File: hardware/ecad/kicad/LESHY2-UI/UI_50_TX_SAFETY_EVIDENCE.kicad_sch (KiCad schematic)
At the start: 0 parts

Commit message: complete exact H2.2.9 UI TX safety schematic
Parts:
- added C1: TDK C1005X7R1H104K050BB, Capacitor_SMD:C_0402_1005Metric, symbol Leshy2:UI50_IR_EVIDENCE_AMP_BYPASS
- added C2: TDK C1005X7R1H104K050BB, Capacitor_SMD:C_0402_1005Metric, symbol Leshy2:UI50_IR_EVIDENCE_VREF_CAP
- added C3: KEMET C0402C102K5RACTU, Capacitor_SMD:C_0402_1005Metric, symbol Leshy2:UI50_IR_EVIDENCE_FEEDBACK_CAP
- added C4: TDK C1005X7R1H104K050BB, Capacitor_SMD:C_0402_1005Metric, symbol Leshy2:UI50_EVIDENCE_CMP_A_BYPASS
- added D1: VEMD1060X01, Leshy2:VEMD1060X01, symbol Leshy2:UI50_DET_IR
- added Q1: Diodes Incorporated 2N7002DW-7-F, Package_TO_SOT_SMD:SOT-363_SC-70-6, symbol Leshy2:UI50_SAFE_RESET_SINK_A
- added R1: Yageo RC0402FR-07100KL, Resistor_SMD:R_0402_1005Metric, symbol Leshy2:UI50_IR_EVIDENCE_VREF_TOP
- added R10: Yageo RC0402FR-0710KL, Resistor_SMD:R_0402_1005Metric, symbol Leshy2:UI50_C5_EVIDENCE_THRESHOLD_BOTTOM
- added R11: Yageo RC0402FR-071ML, Resistor_SMD:R_0402_1005Metric, symbol Leshy2:UI50_C5_EVIDENCE_HYSTERESIS
- added R12: Yageo RC0402FR-0710KL, Resistor_SMD:R_0402_1005Metric, symbol Leshy2:UI50_C5_EVIDENCE_OUTPUT_PULLUP
- added R13: Yageo RC0402FR-07100KL, Resistor_SMD:R_0402_1005Metric, symbol Leshy2:UI50_IR_EVIDENCE_THRESHOLD_TOP
- added R14: Yageo RC0402FR-0712KL, Resistor_SMD:R_0402_1005Metric, symbol Leshy2:UI50_IR_EVIDENCE_THRESHOLD_BOTTOM
- added R15: Yageo RC0402FR-071ML, Resistor_SMD:R_0402_1005Metric, symbol Leshy2:UI50_IR_EVIDENCE_HYSTERESIS
- added R16: Yageo RC0402FR-0710KL, Resistor_SMD:R_0402_1005Metric, symbol Leshy2:UI50_IR_EVIDENCE_OUTPUT_PULLUP
- added R17: Yageo RC0402FR-0710KL, Resistor_SMD:R_0402_1005Metric, symbol Leshy2:UI50_C5_EVIDENCE_MAIN_PULLUP
- added R18: Yageo RC0402FR-0710KL, Resistor_SMD:R_0402_1005Metric, symbol Leshy2:UI50_IR_EVIDENCE_MAIN_PULLUP
- added R2: Yageo RC0402FR-0710KL, Resistor_SMD:R_0402_1005Metric, symbol Leshy2:UI50_IR_EVIDENCE_VREF_BOTTOM
- added R3: Yageo RC0402FR-0747KL, Resistor_SMD:R_0402_1005Metric, symbol Leshy2:UI50_IR_EVIDENCE_FEEDBACK
- added R4: Yageo RC0402FR-0710KL, Resistor_SMD:R_0402_1005Metric, symbol Leshy2:UI50_S3_RESET_GATE_PULLUP
- added R5: Yageo RC0402FR-07100KL, Resistor_SMD:R_0402_1005Metric, symbol Leshy2:UI50_S3_EVIDENCE_THRESHOLD_TOP
- added R6: Yageo RC0402FR-0710KL, Resistor_SMD:R_0402_1005Metric, symbol Leshy2:UI50_S3_EVIDENCE_THRESHOLD_BOTTOM
- added R7: Yageo RC0402FR-071ML, Resistor_SMD:R_0402_1005Metric, symbol Leshy2:UI50_S3_EVIDENCE_HYSTERESIS
- added R8: Yageo RC0402FR-0710KL, Resistor_SMD:R_0402_1005Metric, symbol Leshy2:UI50_S3_EVIDENCE_OUTPUT_PULLUP
- added R9: Yageo RC0402FR-07100KL, Resistor_SMD:R_0402_1005Metric, symbol Leshy2:UI50_C5_EVIDENCE_THRESHOLD_TOP
- added U1: TLV9061IDBVR, Package_TO_SOT_SMD:SOT-23-5, symbol Leshy2:UI50_IR_EVIDENCE_AMP
- added U2: LTC5532ES6#TRMPBF, Package_TO_SOT_SMD:TSOT-23-6, symbol Leshy2:UI50_DET_S3
- added U3: LTC5532ES6#TRMPBF, Package_TO_SOT_SMD:TSOT-23-6, symbol Leshy2:UI50_DET_C5
- added U4: TLV1824PWR, Package_SO:TSSOP-14_4.4x5mm_P0.65mm, symbol Leshy2:UI50_EVIDENCE_CMP_A
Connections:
- net 3V3_MAIN: now also R17.1 (END_1), R18.1 (END_1), R4.1 (END_1)
- net AON_SAFE_3V3: now also C1.1 (END_1), C4.1 (END_1), R1.1 (END_1), R12.1 (END_1), R13.1 (END_1), R16.1 (END_1), R5.1 (END_1), R8.1 (END_1), R9.1 (END_1), U1.5 (V_PLUS), U2.6 (VCC), U3.6 (VCC), U4.3 (VPLUS)
- net C5_DETECT_V: now also U3.5 (VOUT), U4.6 (IN2_N)
- net C5_DETECT_VM: now also U3.4 (VM)
- net C5_FORWARD_RF_SAMPLE: now also U3.1 (RFIN)
- net C5_RESET_N: now also Q1.1 (D2)
- net C5_RF_TX_EVIDENCE_N: now also R17.2 (END_2)
- net EV_N0_S3: now also R7.1 (END_1), R8.2 (END_2), U4.2 (OUT1)
- net EV_N1_C5: now also R11.1 (END_1), R12.2 (END_2), U4.1 (OUT2)
- net EV_N7_IR: now also R15.1 (END_1), R16.2 (END_2), U4.14 (OUT3)
- net IR_TX_EVIDENCE_N: now also R18.2 (END_2)
- net RF_RESET_KILL_GATE: now also Q1.5 (G2)
- net S3_DETECT_V: now also U2.5 (VOUT), U4.4 (IN1_N)
- net S3_DETECT_VM: now also U2.4 (VM)
- net S3_FORWARD_RF_SAMPLE: now also U2.1 (RFIN)
- net S3_RESET_KILL_GATE: now also Q1.2 (G1), R4.2 (END_2)
- net S3_RESET_N: now also Q1.4 (D1)
- net SAFETY_GROUND: now also C1.2 (END_2), C2.2 (END_2), C4.2 (END_2), D1.1 (ANODE), Q1.3 (S1), Q1.6 (S2), R10.2 (END_2), R14.2 (END_2), R2.2 (END_2), R6.2 (END_2), U1.2 (V_MINUS), U2.2 (GND), U2.3 (VOS), U3.2 (GND), U3.3 (VOS), U4.10 (IN4_N), U4.11 (IN4_P), U4.12 (VMINUS)
- new net EV_THRESH_0_S3: R5.2 (END_2), R6.1 (END_1), R7.2 (END_2), U4.5 (IN1_P)
- new net EV_THRESH_1_C5: R10.1 (END_1), R11.2 (END_2), R9.2 (END_2), U4.7 (IN2_P)
- new net EV_THRESH_7_IR: R13.2 (END_2), R14.1 (END_1), R15.2 (END_2), U4.9 (IN3_P)
- new net IR_DETECT_V: C3.1 (END_1), R3.1 (END_1), U1.1 (OUT), U4.8 (IN3_N)
- new net IR_EVIDENCE_VREF: C2.1 (END_1), R1.2 (END_2), R2.1 (END_1), U1.3 (IN_PLUS)
- new net IR_OPTICAL_SUM: C3.2 (END_2), D1.2 (CATHODE), R3.2 (END_2), U1.4 (IN_MINUS)
- no-connect marks 19 -> 1
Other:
- title: (none) -> Leshy2 — exact UI-side actual-TX evidence and reset safety

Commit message: complete H2 schematic review package
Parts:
- renumbered C1 to C50001, C2 to C50002, C3 to C50003, C4 to C50004, D1 to D50001, Q1 to Q50001, R1 to R50001, R2 to R50002, R3 to R50003, R4 to R50004, R5 to R50005, R6 to R50006, R7 to R50007, R8 to R50008, R9 to R50009, R10 to R50010, R11 to R50011, R12 to R50012, R13 to R50013, R14 to R50014, R15 to R50015, R16 to R50016, R17 to R50017, R18 to R50018, U1 to U50001, U2 to U50002, U3 to U50003, U4 to U50004
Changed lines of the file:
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@@
 		(on_board yes)
 		(dnp no)
-		(property "Reference" "U1"
+		(property "Reference" "U50001"
 			(at 50.80 40.64 0)
 			(show_name no)
@@
 			(project "LESHY2-UI"
 				(path "/25ddd286-5916-5146-b4db-5f80ff4b0f07"
-					(reference "U1")
+					(reference "U50001")
 					(unit 1)
 				)
@@
 		(on_board yes)
 		(dnp no)
-		(property "Reference" "C1"
+		(property "Reference" "C50001"
 			(at 132.08 39.37 0)
 			(show_name no)
@@
 			(project "LESHY2-UI"
 				(path "/25ddd286-5916-5146-b4db-5f80ff4b0f07"
-					(reference "C1")
+					(reference "C50001")
 					(unit 1)
 				)
@@
 		(on_board yes)
 		(dnp no)
-		(property "Reference" "R1"
+		(property "Reference" "R50001"
 			(at 213.36 39.37 0)
 			(show_name no)
@@
 			(project "LESHY2-UI"
 				(path "/25ddd286-5916-5146-b4db-5f80ff4b0f07"
-					(reference "R1")
+					(reference "R50001")
 					(unit 1)
 				)
@@
 		(on_board yes)
 		(dnp no)
-		(property "Reference" "R2"
+		(property "Reference" "R50002"
 			(at 294.64 39.37 0)
 			(show_name no)
@@
 			(project "LESHY2-UI"
 				(path "/25ddd286-5916-5146-b4db-5f80ff4b0f07"
-					(reference "R2")
+					(reference "R50002")
 					(unit 1)
 				)
@@
 		(on_board yes)
 		(dnp no)
-		(property "Reference" "C2"
+		(property "Reference" "C50002"
 			(at 375.92 39.37 0)
 			(show_name no)
@@
 			(project "LESHY2-UI"
 				(path "/25ddd286-5916-5146-b4db-5f80ff4b0f07"
-					(reference "C2")
+					(reference "C50002")
 					(unit 1)
 				)
@@
 		(on_board yes)
 		(dnp no)
-		(property "Reference" "R3"
+		(property "Reference" "R50003"
 			(at 457.20 39.37 0)
 			(show_name no)
@@
 			(project "LESHY2-UI"
 				(path "/25ddd286-5916-5146-b4db-5f80ff4b0f07"
-					(reference "R3")
+					(reference "R50003")
 					(unit 1)
 				)
@@
 		(on_board yes)
 		(dnp no)
-		(property "Reference" "C3"
+		(property "Reference" "C50003"
 			(at 132.08 64.77 0)
 			(show_name no)
@@
 			(project "LESHY2-UI"
 				(path "/25ddd286-5916-5146-b4db-5f80ff4b0f07"
-					(reference "C3")
+					(reference "C50003")
 					(unit 1)
 				)
@@
 		(on_board yes)
 		(dnp no)
-		(property "Reference" "R4"
+		(property "Reference" "R50004"
 			(at 213.36 64.77 0)
 			(show_name no)
@@
 			(project "LESHY2-UI"
 				(path "/25ddd286-5916-5146-b4db-5f80ff4b0f07"
-					(reference "R4")
+					(reference "R50004")
 					(unit 1)
 				)
@@
 		(on_board yes)
 		(dnp no)
-		(property "Reference" "Q1"
+		(property "Reference" "Q50001"
 			(at 294.64 66.04 0)
 			(show_name no)
@@
 			(project "LESHY2-UI"
 				(path "/25ddd286-5916-5146-b4db-5f80ff4b0f07"
-					(reference "Q1")
+					(reference "Q50001")
 					(unit 1)
 				)
@@
 		(on_board yes)
 		(dnp no)
-		(property "Reference" "U2"
+		(property "Reference" "U50002"
 			(at 375.92 66.04 0)
 			(show_name no)
@@
 			(project "LESHY2-UI"
 				(path "/25ddd286-5916-5146-b4db-5f80ff4b0f07"
-					(reference "U2")
+					(reference "U50002")
 					(unit 1)
 				)
@@
 		(on_board yes)
 		(dnp no)
-		(property "Reference" "U3"
+		(property "Reference" "U50003"
 			(at 457.20 66.04 0)
 			(show_name no)
@@
 			(project "LESHY2-UI"
 				(path "/25ddd286-5916-5146-b4db-5f80ff4b0f07"
-					(reference "U3")
+					(reference "U50003")
 					(unit 1)
 				)
@@
 		(on_board yes)
 		(dnp no)
-		(property "Reference" "D1"
+		(property "Reference" "D50001"
 			(at 50.80 67.31 0)
 			(show_name no)
@@
 			(project "LESHY2-UI"
 				(path "/25ddd286-5916-5146-b4db-5f80ff4b0f07"
-					(reference "D1")
+					(reference "D50001")
 					(unit 1)
 				)
@@
 		(on_board yes)
 		(dnp no)
-		(property "Reference" "U4"
+		(property "Reference" "U50004"
 			(at 132.08 91.80 0)
 			(show_name no)
@@
 			(project "LESHY2-UI"
 				(path "/25ddd286-5916-5146-b4db-5f80ff4b0f07"
-					(reference "U4")
+					(reference "U50004")
 					(unit 1)
 				)
@@
 		(on_board yes)
 		(dnp no)
-		(property "Reference" "C4"
+		(property "Reference" "C50004"
 			(at 213.36 90.17 0)
 			(show_name no)
@@
 			(project "LESHY2-UI"
 				(path "/25ddd286-5916-5146-b4db-5f80ff4b0f07"
-					(reference "C4")
+					(reference "C50004")
 					(unit 1)
 				)
@@
 		(on_board yes)
 		(dnp no)
-		(property "Reference" "R5"
+		(property "Reference" "R50005"
 			(at 50.80 92.71 0)
 			(show_name no)
@@
 			(project "LESHY2-UI"
 				(path "/25ddd286-5916-5146-b4db-5f80ff4b0f07"
-					(reference "R5")
+					(reference "R50005")
 					(unit 1)
 				)
@@
 		(on_board yes)
 		(dnp no)
-		(property "Reference" "R6"
+		(property "Reference" "R50006"
 			(at 294.64 92.71 0)
 			(show_name no)
@@
 			(project "LESHY2-UI"
 				(path "/25ddd286-5916-5146-b4db-5f80ff4b0f07"
-					(reference "R6")
+					(reference "R50006")
 					(unit 1)
 				)
@@
 		(on_board yes)
 		(dnp no)
-		(property "Reference" "R7"
+		(property "Reference" "R50007"
 			(at 375.92 92.71 0)
 			(show_name no)
@@
 			(project "LESHY2-UI"
 				(path "/25ddd286-5916-5146-b4db-5f80ff4b0f07"
-					(reference "R7")
+					(reference "R50007")
 					(unit 1)
 				)
@@
 		(on_board yes)
 		(dnp no)
-		(property "Reference" "R8"
+		(property "Reference" "R50008"
 			(at 457.20 92.71 0)
 			(show_name no)
@@
 			(project "LESHY2-UI"
 				(path "/25ddd286-5916-5146-b4db-5f80ff4b0f07"
-					(reference "R8")
+					(reference "R50008")
 					(unit 1)
 				)
@@
 		(on_board yes)
 		(dnp no)
-		(property "Reference" "R9"
+		(property "Reference" "R50009"
 			(at 213.36 115.57 0)
 			(show_name no)
@@
 			(project "LESHY2-UI"
 				(path "/25ddd286-5916-5146-b4db-5f80ff4b0f07"
-					(reference "R9")
+					(reference "R50009")
 					(unit 1)
 				)
@@
 		(on_board yes)
 		(dnp no)
-		(property "Reference" "R10"
+		(property "Reference" "R50010"
 			(at 50.80 118.11 0)
 			(show_name no)
@@
 			(project "LESHY2-UI"
 				(path "/25ddd286-5916-5146-b4db-5f80ff4b0f07"
-					(reference "R10")
+					(reference "R50010")
 					(unit 1)
 				)
@@
 		(on_board yes)
 		(dnp no)
-		(property "Reference" "R11"
+		(property "Reference" "R50011"
 			(at 294.64 118.11 0)
 			(show_name no)
@@
 			(project "LESHY2-UI"
 				(path "/25ddd286-5916-5146-b4db-5f80ff4b0f07"
-					(reference "R11")
+					(reference "R50011")
 					(unit 1)
 				)
@@
 		(on_board yes)
 		(dnp no)
-		(property "Reference" "R12"
+		(property "Reference" "R50012"
 			(at 375.92 118.11 0)
 			(show_name no)
@@
 			(project "LESHY2-UI"
 				(path "/25ddd286-5916-5146-b4db-5f80ff4b0f07"
-					(reference "R12")
+					(reference "R50012")
 					(unit 1)
 				)
@@
 		(on_board yes)
 		(dnp no)
-		(property "Reference" "R13"
+		(property "Reference" "R50013"
 			(at 457.20 118.11 0)
 			(show_name no)
@@
 			(project "LESHY2-UI"
 				(path "/25ddd286-5916-5146-b4db-5f80ff4b0f07"
-					(reference "R13")
+					(reference "R50013")
 					(unit 1)
 				)
@@
 		(on_board yes)
 		(dnp no)
-		(property "Reference" "R14"
+		(property "Reference" "R50014"
 			(at 132.08 128.27 0)
 			(show_name no)
@@
 			(project "LESHY2-UI"
 				(path "/25ddd286-5916-5146-b4db-5f80ff4b0f07"
-					(reference "R14")
+					(reference "R50014")
 					(unit 1)
 				)
@@
 		(on_board yes)
 		(dnp no)
-		(property "Reference" "R15"
+		(property "Reference" "R50015"
 			(at 213.36 140.97 0)
 			(show_name no)
@@
 			(project "LESHY2-UI"
 				(path "/25ddd286-5916-5146-b4db-5f80ff4b0f07"
-					(reference "R15")
+					(reference "R50015")
 					(unit 1)
 				)
@@
 		(on_board yes)
 		(dnp no)
-		(property "Reference" "R16"
+		(property "Reference" "R50016"
 			(at 50.80 143.51 0)
 			(show_name no)
@@
 			(project "LESHY2-UI"
 				(path "/25ddd286-5916-5146-b4db-5f80ff4b0f07"
-					(reference "R16")
+					(reference "R50016")
 					(unit 1)
 				)
@@
 		(on_board yes)
 		(dnp no)
-		(property "Reference" "R17"
+		(property "Reference" "R50017"
 			(at 294.64 143.51 0)
 			(show_name no)
@@
 			(project "LESHY2-UI"
 				(path "/25ddd286-5916-5146-b4db-5f80ff4b0f07"
-					(reference "R17")
+					(reference "R50017")
 					(unit 1)
 				)
@@
 		(on_board yes)
 		(dnp no)
-		(property "Reference" "R18"
+		(property "Reference" "R50018"
 			(at 375.92 143.51 0)
 			(show_name no)
@@
 			(project "LESHY2-UI"
 				(path "/25ddd286-5916-5146-b4db-5f80ff4b0f07"
-					(reference "R18")
-					(unit 1)
-				)
+					(reference "R50018")
+					(unit 1)
+				)

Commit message: review H3.6.2 single-fault containment
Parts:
- added C50004: TDK C1005X7R1H104K050BB, Capacitor_SMD:C_0402_1005Metric, symbol Leshy2:UI50_SAFE_C5_RESET_BUFFER_BYPASS
- added C50005: TDK C1005X7R1H104K050BB, Capacitor_SMD:C_0402_1005Metric, symbol Leshy2:UI50_SAFE_C5_FAULT_RESET_BUFFER_BYPASS
- added R50004: Yageo RC0402FR-0710KL, Resistor_SMD:R_0402_1005Metric, symbol Leshy2:UI50_SAFE_C5_RESET_GATE_PULLUP
- added U50002: Texas Instruments SN74LVC1G06DCKR, Package_TO_SOT_SMD:SOT-353_SC-70-5, symbol Leshy2:UI50_SAFE_C5_RESET_BUFFER
- added U50003: SN74LVC1G07DCKR, Package_TO_SOT_SMD:SOT-353_SC-70-5, symbol Leshy2:UI50_SAFE_C5_FAULT_RESET_BUFFER
- renumbered C50004 to C50006, R50004 to R50005, R50005 to R50006, R50006 to R50007, R50007 to R50008, R50008 to R50009, R50009 to R50010, R50010 to R50011, R50011 to R50012, R50012 to R50013, R50013 to R50014, R50014 to R50015, R50015 to R50016, R50016 to R50017, R50017 to R50018, R50018 to R50019, U50002 to U50004, U50003 to U50005, U50004 to U50006
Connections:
- net 3V3_MAIN: now also R50004.1 (END_1)
- net AON_SAFE_3V3: now also C50004.1 (END_1), C50005.1 (END_1), U50002.5 (VCC), U50003.5 (VCC)
- net C5_RESET_N: now also U50003.4 (Y)
- net SAFETY_GROUND: now also C50004.2 (END_2), C50005.2 (END_2), U50002.3 (GND), U50003.3 (GND)
- net RF_RESET_KILL_GATE renamed C5_RESET_KILL_GATE
- net C5_RESET_KILL_GATE: now also R50004.2 (END_2), U50002.4 (Y)
- new net FAULT_ASSERT_N: U50003.2 (A)
- new net RUN_PERMIT: U50002.2 (A)
- no-connect marks 1 -> 3
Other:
- moved on the sheet: C50006, D50001, Q50001, R50005, R50006, R50007, R50008, R50009, R50010, R50011, R50012, R50013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

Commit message: Optimize H1 display and stocked BOM routes
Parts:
- C50001, C50002, C50004, C50005, C50006: value TDK C1005X7R1H104K050BB -> Yageo CC0402KRX7R9BB104
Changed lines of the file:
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@@
 			(effects (font (size 1.27 1.27)))
 		)
-		(property "Value" "TDK C1005X7R1H104K050BB"
+		(property "Value" "Yageo CC0402KRX7R9BB104"
 			(at 132.08 49.53 0)
 			(show_name no)
@@
 			(effects (font (size 1.27 1.27)))
 		)
-		(property "Value" "TDK C1005X7R1H104K050BB"
+		(property "Value" "Yageo CC0402KRX7R9BB104"
 			(at 375.92 49.53 0)
 			(show_name no)
@@
 			(effects (font (size 1.27 1.27)))
 		)
-		(property "Value" "TDK C1005X7R1H104K050BB"
+		(property "Value" "Yageo CC0402KRX7R9BB104"
 			(at 294.64 74.93 0)
 			(show_name no)
@@
 			(effects (font (size 1.27 1.27)))
 		)
-		(property "Value" "TDK C1005X7R1H104K050BB"
+		(property "Value" "Yageo CC0402KRX7R9BB104"
 			(at 50.80 77.47 0)
 			(show_name no)
@@
 			(effects (font (size 1.27 1.27)))
 		)
-		(property "Value" "TDK C1005X7R1H104K050BB"
+		(property "Value" "Yageo CC0402KRX7R9BB104"
 			(at 132.08 125.73 0)
 			(show_name no)

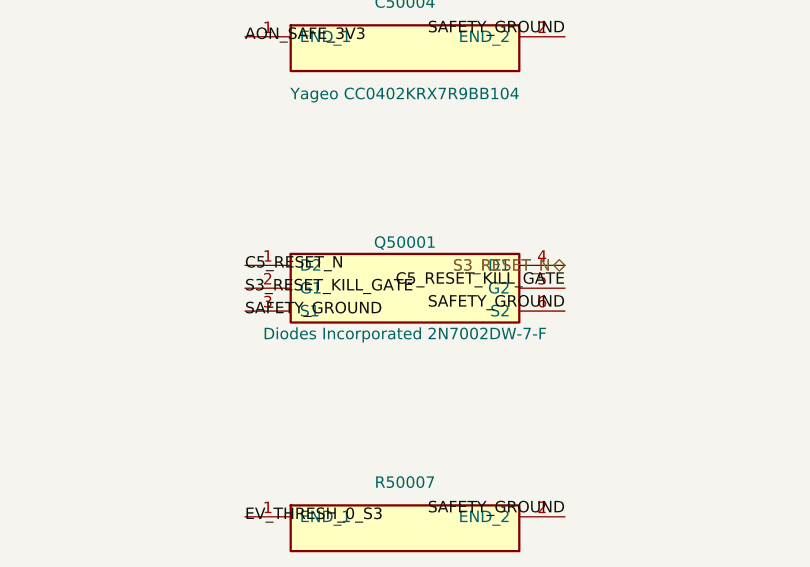
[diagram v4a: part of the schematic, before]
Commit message: Correct dual-NMOS physical pin mapping
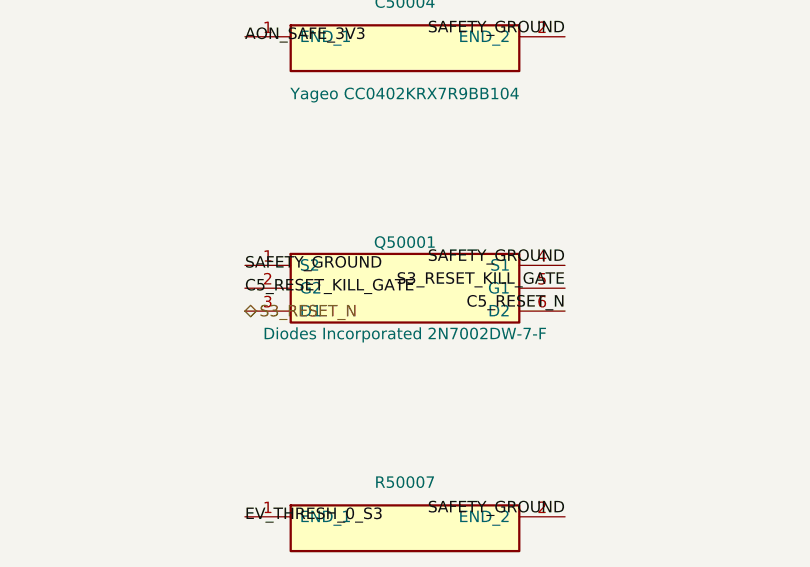
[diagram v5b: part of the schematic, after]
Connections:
- net C5_RESET_KILL_GATE: now also Q50001.2 (G2); no longer Q50001.5 (G2)
- net C5_RESET_N: now also Q50001.6 (D2); no longer Q50001.1 (D2)
- net S3_RESET_KILL_GATE: now also Q50001.5 (G1); no longer Q50001.2 (G1)
- net S3_RESET_N: now also Q50001.3 (D1); no longer Q50001.4 (D1)
- net SAFETY_GROUND: now also Q50001.1 (S2), Q50001.4 (S1); no longer Q50001.3 (S1), Q50001.6 (S2)
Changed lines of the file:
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@@
 	)
 	(label "C5_RESET_KILL_GATE"
-		(at 312.42 96.52 180)
-		(effects (font (size 1.27 1.27)) (justify right bottom))
+		(at 276.86 96.52 0)
+		(effects (font (size 1.27 1.27)))
 	)
 	(hierarchical_label "C5_RESET_N"
@@
 	)
 	(label "C5_RESET_N"
-		(at 276.86 93.98 0)
-		(effects (font (size 1.27 1.27)))
+		(at 312.42 99.06 180)
+		(effects (font (size 1.27 1.27)) (justify right bottom))
 	)
 	(hierarchical_label "C5_RF_TX_EVIDENCE_N"
@@
 	)
 	(label "S3_RESET_KILL_GATE"
-		(at 276.86 96.52 0)
-		(effects (font (size 1.27 1.27)))
+		(at 312.42 96.52 180)
+		(effects (font (size 1.27 1.27)) (justify right bottom))
 	)
 	(hierarchical_label "S3_RESET_N"
 		(shape bidirectional)
+		(at 276.86 99.06 0)
+		(effects (font (size 1.27 1.27)))
+	)
+	(hierarchical_label "SAFETY_GROUND"
+		(shape bidirectional)
+		(at 33.02 45.72 0)
+		(effects (font (size 1.27 1.27)))
+	)
+	(label "SAFETY_GROUND"
+		(at 149.86 43.18 180)
+		(effects (font (size 1.27 1.27)) (justify right bottom))
+	)
+	(label "SAFETY_GROUND"
+		(at 312.42 43.18 180)
+		(effects (font (size 1.27 1.27)) (justify right bottom))
+	)
+	(label "SAFETY_GROUND"
+		(at 393.70 43.18 180)
+		(effects (font (size 1.27 1.27)) (justify right bottom))
+	)
+	(label "SAFETY_GROUND"
+		(at 195.58 73.66 0)
+		(effects (font (size 1.27 1.27)))
+	)
+	(label "SAFETY_GROUND"
+		(at 312.42 68.58 180)
+		(effects (font (size 1.27 1.27)) (justify right bottom))
+	)
+	(label "SAFETY_GROUND"
+		(at 439.42 73.66 0)
+		(effects (font (size 1.27 1.27)))
+	)
+	(label "SAFETY_GROUND"
+		(at 68.58 71.12 180)
+		(effects (font (size 1.27 1.27)) (justify right bottom))
+	)
+	(label "SAFETY_GROUND"
+		(at 276.86 93.98 0)
+		(effects (font (size 1.27 1.27)))
+	)
+	(label "SAFETY_GROUND"
 		(at 312.42 93.98 180)
 		(effects (font (size 1.27 1.27)) (justify right bottom))
 	)
-	(hierarchical_label "SAFETY_GROUND"
-		(shape bidirectional)
-		(at 33.02 45.72 0)
-		(effects (font (size 1.27 1.27)))
-	)
-	(label "SAFETY_GROUND"
-		(at 149.86 43.18 180)
-		(effects (font (size 1.27 1.27)) (justify right bottom))
-	)
-	(label "SAFETY_GROUND"
-		(at 312.42 43.18 180)
-		(effects (font (size 1.27 1.27)) (justify right bottom))
-	)
-	(label "SAFETY_GROUND"
-		(at 393.70 43.18 180)
-		(effects (font (size 1.27 1.27)) (justify right bottom))
-	)
-	(label "SAFETY_GROUND"
-		(at 195.58 73.66 0)
-		(effects (font (size 1.27 1.27)))
-	)
-	(label "SAFETY_GROUND"
-		(at 312.42 68.58 180)
-		(effects (font (size 1.27 1.27)) (justify right bottom))
-	)
-	(label "SAFETY_GROUND"
-		(at 439.42 73.66 0)
-		(effects (font (size 1.27 1.27)))
-	)
-	(label "SAFETY_GROUND"
-		(at 68.58 71.12 180)
-		(effects (font (size 1.27 1.27)) (justify right bottom))
-	)
-	(label "SAFETY_GROUND"
-		(at 276.86 99.06 0)
-		(effects (font (size 1.27 1.27)))
-	)
-	(label "SAFETY_GROUND"
-		(at 312.42 99.06 180)
-		(effects (font (size 1.27 1.27)) (justify right bottom))
-	)
